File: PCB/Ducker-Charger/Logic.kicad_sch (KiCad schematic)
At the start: 47 parts, among them CN1 C_Pack04, IC2 TPS54202HDDCT, J6 Debug, J7 Conn_01x08, J8 Conn_01x07, SW1 EC11E15244G1, U7 STM32F401RBT6, Y1 16MHz

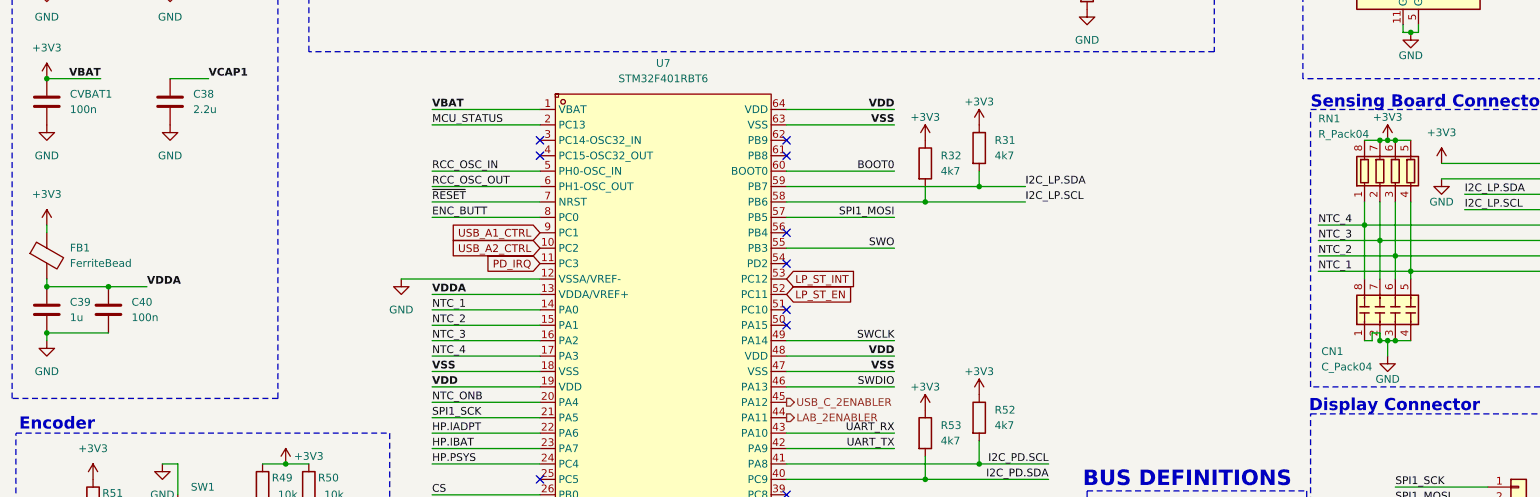
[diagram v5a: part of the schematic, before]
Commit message: feat: splitted analog line
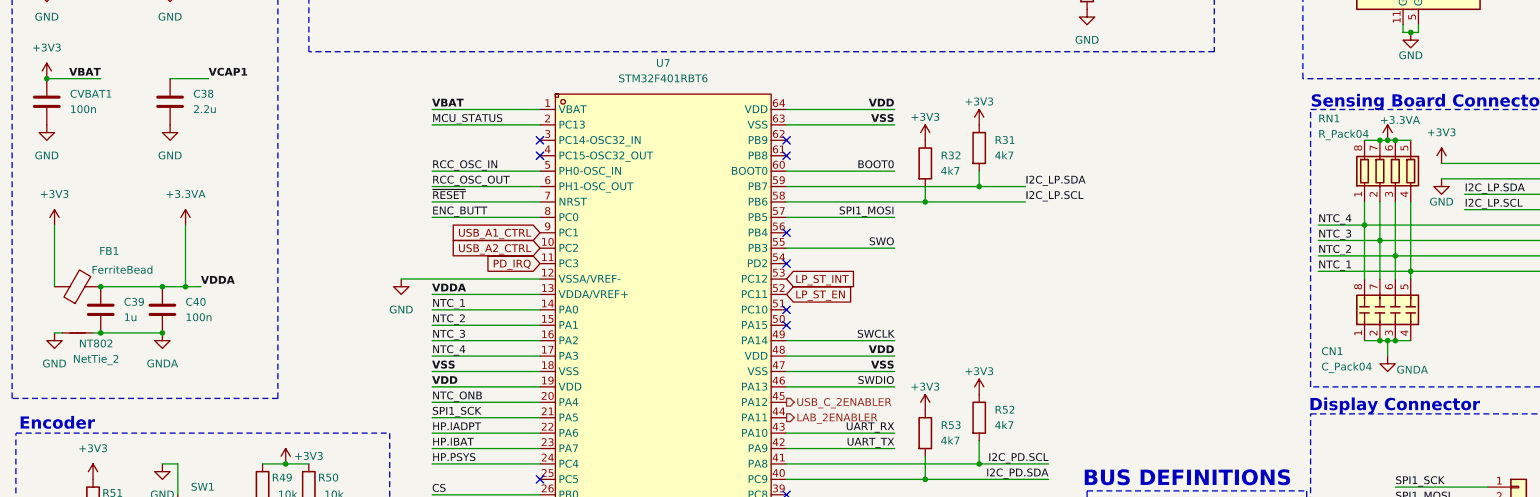
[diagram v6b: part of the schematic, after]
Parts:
- added NT802: NetTie_2, NetTie:NetTie-2_SMD_Pad0.5mm, symbol Device:NetTie_2
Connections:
- net +3V3: no longer RN1.5 (R4.2), RN1.6 (R3.2), RN1.7 (R2.2), RN1.8 (R1.2)
- net GND: now also NT802.1; no longer C39.2, C40.2, CN1.1 (R1.1), CN1.2 (R2.1), CN1.3 (R3.1), CN1.4 (R4.1)
- net VDDA renamed +3.3VA
- net +3.3VA: now also RN1.5 (R4.2), RN1.6 (R3.2), RN1.7 (R2.2), RN1.8 (R1.2)
- new net GNDA: C39.2, C40.2, CN1.1 (R1.1), CN1.2 (R2.1), CN1.3 (R3.1), CN1.4 (R4.1), NT802.2
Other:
- moved on the sheet: C39, C40, FB1

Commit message: feat: remade the PCB & minor schematic fixes
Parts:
- removed J8: Conn_01x07, Connector_JST:JST_XH_S7B-XH-A_1x07_P2.50mm_Horizontal, symbol Connector_Generic:Conn_01x07
- removed R27: 100k, Resistor_SMD:R_0603_1608Metric, symbol Device:R
- added C415, C420: 100n, Capacitor_SMD:C_0603_1608Metric, symbol Device:C
- added J404: Conn_01x08, Connector_JST:JST_EH_B8B-EH-A_1x08_P2.50mm_Vertical, symbol Connector_Generic:Conn_01x08
- added JP402: BL_NODE, Jumper:SolderJumper-3_P1.3mm_Open_RoundedPad1.0x1.5mm, symbol Jumper:SolderJumper_3_Open
- added Q401: AO3400A, EasyEDA:SOT-23-3_L2.9-W1.3-P1.90-LS2.4-BR, symbol EasyEDA:AO3400A
- added Q402: PMOS, EasyEDA:SOT-23-3_L2.9-W1.3-P1.90-LS2.4-BR, symbol Simulation_SPICE:PMOS
- added R415, R417, R419: 10k, Resistor_SMD:R_0603_1608Metric, symbol Device:R
- added R416, R418: 1k, Resistor_SMD:R_0603_1608Metric, symbol Device:R
- added R420: 4k7, Resistor_SMD:R_0603_1608Metric, symbol Device:R
- added SW403: Reset, Button_Switch_SMD:SW_SPST_FSMSM, symbol Switch:SW_Push
- added TH401: Thermistor_NTC, Resistor_SMD:R_0603_1608Metric, symbol Device:Thermistor_NTC
- C413: renamed from C31; value 10u -> 10u 25V; footprint Capacitor_SMD:C_0805_2012Metric -> Capacitor_SMD:C_1206_3216Metric
- C416: renamed from C28; value 0.1u -> 100n
- CN401: renamed from CN1; value C_Pack04 -> 100n
- R402: renamed from R33; value 1k -> 220
- R414: renamed from R30; value 0 -> 4k87
- RN401: renamed from RN1; value R_Pack04 -> 10k
- renumbered C29 to C401, C36 to C402, C53 to C403, C39 to C404, C40 to C405, C30 to C406, C37 to C407, C38 to C408, C41 to C409, C51 to C410, C52 to C411, C42 to C412, C32 to C414, C33 to C417, C34 to C418, C35 to C419, CVBAT1 to CVBAT401, D21 to D401, FB1 to FB401, IC2 to IC401, J6 to J401, J7 to J403, JP1 to JP401, L5 to L401, NT802 to NT401, R51 to R401, R49 to R403, R50 to R404, R26 to R405, R28 to R406, R34 to R407, R54 to R408, R32 to R409, R53 to R410, R31 to R411, R52 to R412, R29 to R413, SW1 to SW401, U7 to U401, Y1 to Y401
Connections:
- net +3.3VA: now also J403.8 (Pin_8), R415.1
- net +3V3: now also C419.2, R413.1, J404.2 (Pin_2), Q402.3 (S), R419.2, R420.1; no longer J403.8 (Pin_8)
- net CS: now also J404.7 (Pin_7)
- net DC: now also J404.6 (Pin_6)
- net GND: now also C415.2, J404.1 (Pin_1), Q401.2 (S), R417.2, SW403.2; no longer J403.7 (Pin_7)
- net GNDA: now also J403.7 (Pin_7), C420.2, TH401.2
- net HP.PD_IRQ: now also R420.2
- net NTC_1: now also J403.4 (Pin_4); no longer J403.1 (Pin_1)
- net NTC_2: now also J403.3 (Pin_3); no longer J403.2 (Pin_2)
- net NTC_3: now also J403.2 (Pin_2); no longer J403.3 (Pin_3)
- net NTC_4: now also J403.1 (Pin_1); no longer J403.4 (Pin_4)
- net NTC_ONB: now also C420.1, R415.2, TH401.1
- net RST: now also J404.5 (Pin_5)
- net SPI1_MOSI: now also J404.4 (Pin_4)
- net SPI1_SCK: now also J404.3 (Pin_3)
- net ~{RESET}: now also C415.1, SW403.1
- net BCKL_CTRL: now reaches U401.61 (PB8)
- net BCKL_CTRL: now also JP402.2 (C)
- net LAB_2ENABLER renamed C2.LAB_EN
- net LP_ST_EN renamed C2.ST_EN
- net LP_ST_INT renamed C2.ST_INT
- net PD_IRQ renamed C2.RDY
- net USB_A1_CTRL renamed USBA.1_CTRL
- net USB_A2_CTRL renamed USBA.2_CTRL
- net USB_C_2ENABLER renamed C2.PORT_EN
- new net: JP402.3 (B), R418.1
- new net: Q402.2 (G), R418.2, R419.1
- new net: JP402.1 (A), R416.1
- new net: Q401.1 (G), R416.2, R417.1
- new net BL: J404.8 (Pin_8), Q401.3 (D), Q402.1 (D)
- no-connect marks 14 -> 13
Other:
- note added: "Onboard NTC"
- moved on the sheet: C403, C409, C410, C411, C412, C413, C414, C416, C417, C418, C419, CN401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
